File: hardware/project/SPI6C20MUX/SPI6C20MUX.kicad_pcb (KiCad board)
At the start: 4 copper layers, 160 x 100 mm, 93 parts, among them J201 5499141-4, J301 Conn_01x06, J302 Conn_02x08_Odd_Even, K201 HE3621A0510, K202 HE3621A0510, K203 HE3621A0510, K204 HE3621A0510, K205 HE3621A0510, K206 HE3621A0510, K207 HE3621A0510, K208 HE3621A0510, K209 HE3621A0510, K210 HE3621A0510, K211 HE3621A0510, K212 HE3621A0510, K213 HE3621A0510, K214 HE3621A0510, K215 HE3621A0510, K216 HE3621A0510, K217 HE3621A0510, K218 HE3621A0510, K219 HE3621A0510, K220 HE3621A0510, K221 HE3621A0510, K222 HE3621A0510, K223 HE3621A0510, K224 HE3621A0510, K225 HE3621A0510, K226 HE3621A0510, K227 HE3621A0510, K228 HE3621A0510, K229 HE3621A0510, K230 HE3621A0510, K231 HE3621A0510, K232 HE3621A0510, K233 HE3621A0510, K234 HE3621A0510, K235 HE3621A0510, K236 HE3621A0510, K237 HE3621A0510, K238 HE3621A0510, K239 HE3621A0510, K240 HE3621A0510, K241 HE3621A0510, K242 HE3621A0510, K243 HE3621A0510, K244 HE3621A0510, K245 HE3621A0510, K246 HE3621A0510, K247 HE3621A0510, K248 HE3621A0510, K249 HE3621A0510, K250 HE3621A0510, K251 HE3621A0510, K252 HE3621A0510, K253 HE3621A0510, K254 HE3621A0510, K255 HE3621A0510, K256 HE3621A0510, K257 HE3621A0510, K258 HE3621A0510, K259 HE3621A0510, K260 HE3621A0510, K261 HE3621A0510, K262 HE3621A0510, K263 HE3621A0510, K264 HE3621A0510, K265 HE3621A0510, K266 HE3621A0510, U201 MCZ33996, U202 MCZ33996, U203 MCZ33996, U204 MCZ33996, U205 MCZ33996, U401 LM1117MPX-3.3

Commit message: Software and hardware development
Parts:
- added R301: 10k, Resistor_SMD:R_0603_1608Metric_Pad1.05x0.95mm_HandSolder, B.Cu at (134.5, 135.3)
- added R302: 10k, Resistor_SMD:R_0603_1608Metric_Pad1.05x0.95mm_HandSolder, B.Cu at (139.4, 135.3)
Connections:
- J302 pad 10: (no net) -> Net-(J302-Pad10)
- U201 pad 30: (no net) -> Net-(U201-Pad30)
- U201 pad 32: (no net) -> Net-(U201-Pad32)
- U202 pad 30: (no net) -> Net-(U202-Pad30)
- U202 pad 32: (no net) -> Net-(U202-Pad32)
- U203 pad 30: (no net) -> Net-(U203-Pad30)
- U203 pad 32: (no net) -> Net-(U203-Pad32)
- U204 pad 12: (no net) -> Net-(U204-Pad12)
- U204 pad 13: (no net) -> Net-(U204-Pad13)
- U204 pad 15: (no net) -> Net-(U204-Pad15)
- U204 pad 16: (no net) -> Net-(U204-Pad16)
- U204 pad 17: (no net) -> Net-(U204-Pad17)
- U204 pad 30: (no net) -> Net-(U204-Pad30)
- U204 pad 32: (no net) -> Net-(U204-Pad32)
- U204 pad 5: (no net) -> Net-(U204-Pad5)
- U205 pad 15: (no net) -> Net-(U205-Pad15)
- U205 pad 16: (no net) -> Net-(U205-Pad16)
- U205 pad 17: (no net) -> Net-(U205-Pad17)
- U205 pad 30: (no net) -> Net-(U205-Pad30)
- U205 pad 32: (no net) -> Net-(U205-Pad32)
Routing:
- net +3V3: track 61.0 -> 68.7 mm

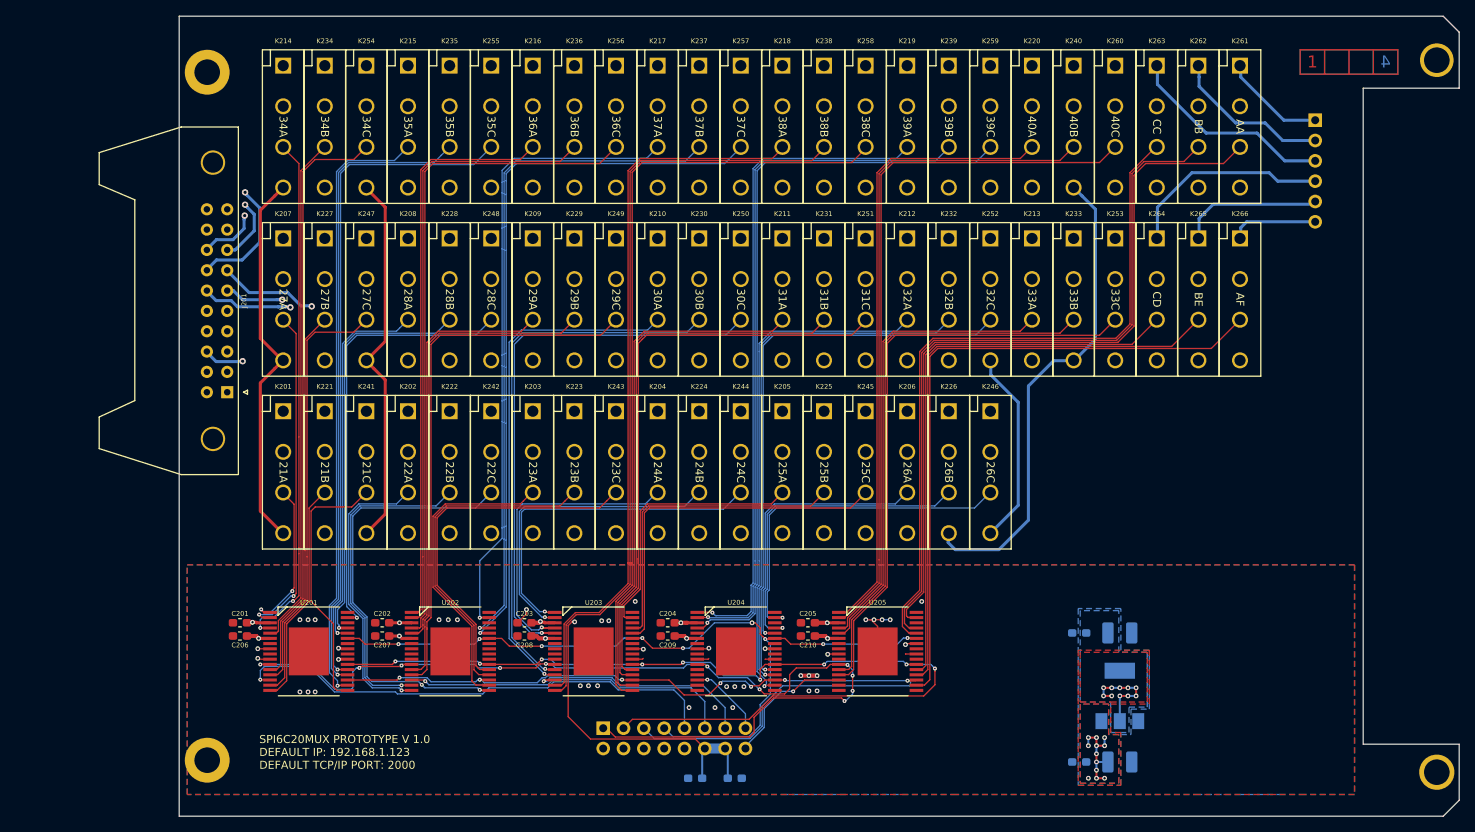
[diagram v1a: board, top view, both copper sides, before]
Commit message: PCB main and module layout.
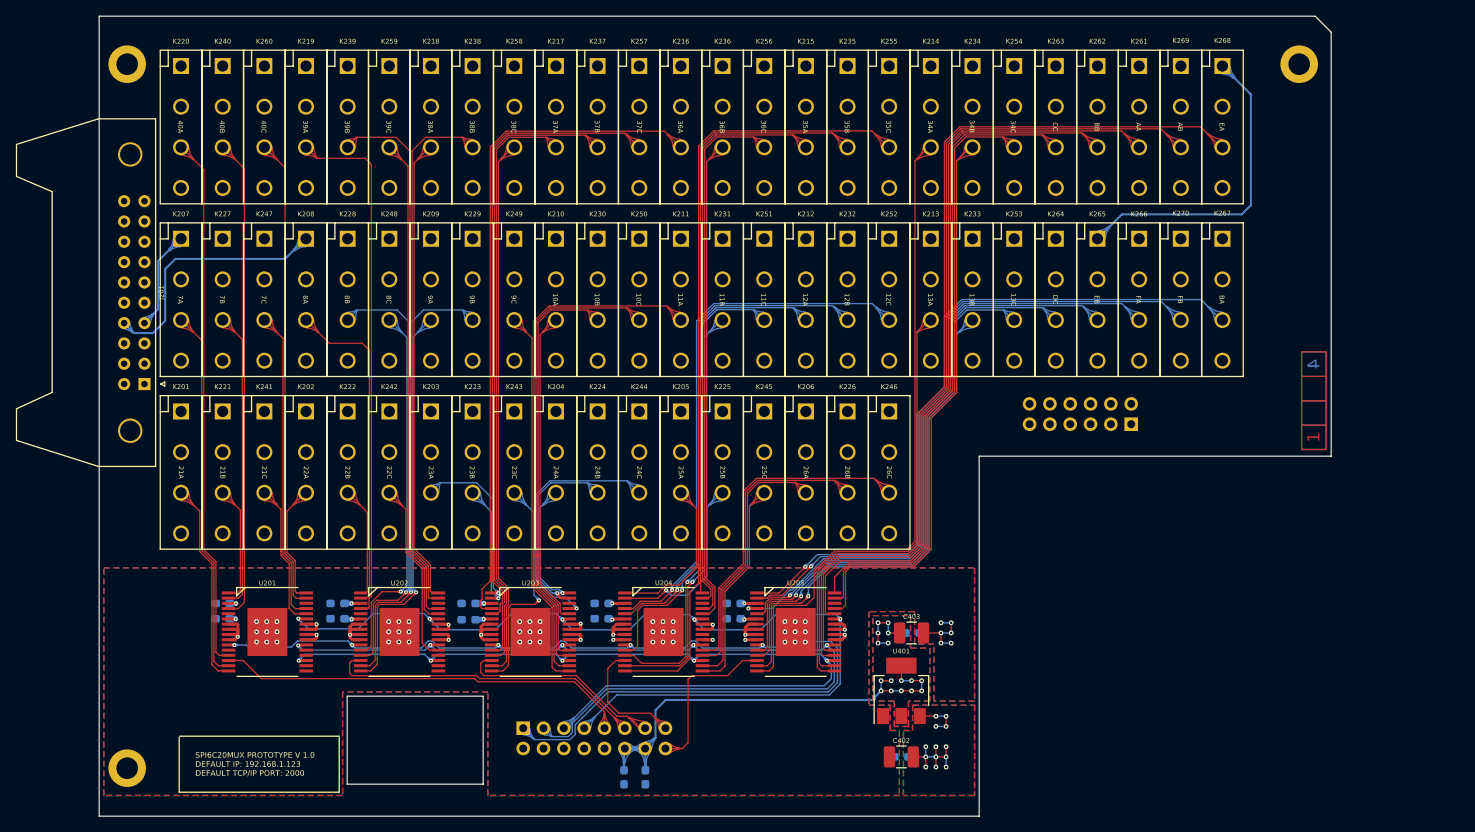
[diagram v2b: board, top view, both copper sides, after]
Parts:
- removed H104: MountingHole, MountingHole:MountingHole_3.2mm_M3_DIN965_Pad
- added K267: HE3621A0510, ETH6C20MUX:HE360_x-5331272-5, F.Cu at (200.4, 75.4)
- added K268: HE3621A0510, ETH6C20MUX:HE360_x-5331272-5, F.Cu at (200.4, 53.8)
- added K269: HE3621A0510, ETH6C20MUX:HE360_x-5331272-5, F.Cu at (195.2, 53.8)
- added K270: HE3621A0510, ETH6C20MUX:HE360_x-5331272-5, F.Cu at (195.2, 75.4)
- C201, C202, C203, C204, C205, C206, C207, C208, C209, C210: moved to B.Cu
- C402, C403, U401: moved to F.Cu
- H101, H102, H103: footprint MountingHole:MountingHole_3.2mm_M3_DIN965_Pad -> MountingHole:MountingHole_2.7mm_M2.5_DIN965_Pad
- J301: value Conn_01x06 -> Conn_02x06_Odd_Even; footprint Connector_PinHeader_2.54mm:PinHeader_1x06_P2.54mm_Vertical -> Connector_PinHeader_2.54mm:PinHeader_2x06_P2.54mm_Vertical
- moved K220 106.4 mm to (70.2, 53.8)
- moved K240 106.4 mm to (75.4, 53.8)
- moved K260 106.4 mm to (80.6, 53.8)
- moved K254 81.0 mm to (174.4, 53.8)
- moved K234 81.0 mm to (169.2, 53.8)
- moved K214 81.0 mm to (164.0, 53.8)
- moved K219 75.1 mm to (85.9, 53.8)
- moved K239 75.1 mm to (91.1, 53.8)
- moved K259 75.1 mm to (96.3, 53.8)
- moved K255 49.8 mm to (158.8, 53.8)
- moved K215 49.7 mm to (148.3, 53.8)
- moved K235 49.7 mm to (153.5, 53.8)
- moved J301 44.4 mm to (189.0, 91.0), turned to 90 degrees
- moved K218 43.9 mm to (101.5, 53.8)
- moved K238 43.9 mm to (106.7, 53.8)
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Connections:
- J301 pad 2: /Connector/B -> /Connector/A
- J301 pad 3: /Connector/C -> /Connector/B
- J301 pad 4: /Connector/D -> /Connector/B
- J301 pad 5: /Connector/E -> /Connector/C
- J301 pad 6: /Connector/F -> /Connector/C
- J302 pad 10: Net-(J302-Pad10) -> (no net)
- U201 pad 1: /Relays/RELAY21A -> /Relays/RELAY21B
- U201 pad 12: /Relays/RELAY34C -> (no net)
- U201 pad 13: /Relays/RELAY27B -> /Relays/RELAY40A
- U201 pad 15: /Relays/RELAY27C -> /Relays/RELAY27A
- U201 pad 16: /Relays/RELAY21B -> /Relays/RELAY21A
- U201 pad 17: /Relays/RELAY21C -> (no net)
- U201 pad 18: /Relays/RELAY35A -> (no net)
- U201 pad 2: /Relays/RELAY27A -> /Relays/RELAY27B
- U201 pad 20: /Relays/RELAY35B -> (no net)
- U201 pad 21: /Relays/RELAY35C -> (no net)
- U201 pad 28: /Relays/RELAY28A -> /Relays/RELAY21C
- U201 pad 29: /Relays/RELAY28B -> /Relays/RELAY27C
- U201 pad 30: Net-(U201-Pad30) -> (no net)
- U201 pad 31: /Relays/RELAY28C -> /Relays/RELAY40C
- U201 pad 32: Net-(U201-Pad32) -> /Relays/RELAY22A
- U201 pad 4: /Relays/RELAY34A -> /Relays/RELAY40B
- U201 pad 5: /Relays/RELAY34B -> (no net)
- U202 pad 1: /Relays/RELAY36A -> /Relays/RELAY22B
- U202 pad 12: /Relays/RELAY29B -> /Relays/RELAY28C
- U202 pad 13: /Relays/RELAY29C -> /Relays/RELAY28B
- U202 pad 15: /Relays/RELAY22B -> /Relays/RELAY29B
- U202 pad 16: /Relays/RELAY22A -> /Relays/RELAY29A
- U202 pad 17: /Relays/RELAY22C -> (no net)
- U202 pad 18: /Relays/RELAY23A -> (no net)
- U202 pad 2: /Relays/RELAY36B -> /Relays/RELAY28A
- U202 pad 20: /Relays/RELAY23B -> (no net)
- U202 pad 21: /Relays/RELAY23C -> /Relays/RELAY22C
- U202 pad 28: /Relays/RELAY37C -> /Relays/RELAY39C
- U202 pad 29: /Relays/RELAY37B -> /Relays/RELAY39B
- U202 pad 30: Net-(U202-Pad30) -> (no net)
- U202 pad 31: /Relays/RELAY37A -> /Relays/RELAY38B
- U202 pad 32: Net-(U202-Pad32) -> /Relays/RELAY38A
- U202 pad 4: /Relays/RELAY36C -> /Relays/RELAY39A
- U202 pad 5: /Relays/RELAY29A -> (no net)
- U203 pad 1: /Relays/RELAY24C -> /Relays/RELAY23A
- U203 pad 12: /Relays/RELAY30B -> /Relays/RELAY37B
- U203 pad 13: /Relays/RELAY30A -> /Relays/RELAY37A
- U203 pad 15: /Relays/RELAY38A -> /Relays/RELAY38C
- U203 pad 16: /Relays/RELAY38B -> /Relays/RELAY23C
- U203 pad 17: /Relays/RELAY38C -> /Relays/RELAY29C
- U203 pad 2: /Relays/RELAY24B -> /Relays/RELAY23B
- U203 pad 20: /Relays/RELAY31B -> /Relays/RELAY30C
- U203 pad 21: /Relays/RELAY31C -> /Relays/RELAY30B
- U203 pad 28: /Relays/RELAY25C -> /Relays/RELAY30A
- U203 pad 29: /Relays/RELAY25B -> /Relays/RELAY24C
- U203 pad 30: Net-(U203-Pad30) -> (no net)
- U203 pad 31: /Relays/RELAY25A -> /Relays/RELAY24B
- U203 pad 32: Net-(U203-Pad32) -> /Relays/RELAY24A
- U203 pad 4: /Relays/RELAY24A -> /Relays/RELAY36A
- U203 pad 5: /Relays/RELAY30C -> /Relays/RELAY37C
- U204 pad 1: /Relays/RELAY39A -> /Relays/RELAY25A
- U204 pad 12: Net-(U204-Pad12) -> /Relays/RELAY32A
- U204 pad 13: Net-(U204-Pad13) -> /Relays/RELAY31C
- U204 pad 15: Net-(U204-Pad15) -> /Relays/RELAY31B
- U204 pad 16: Net-(U204-Pad16) -> /Relays/RELAY35C
- U204 pad 17: Net-(U204-Pad17) -> /Relays/RELAY25C
- U204 pad 18: /Relays/RELAY32A -> /Relays/RELAY26A
- U204 pad 2: /Relays/RELAY39B -> /Relays/RELAY25B
- U204 pad 20: /Relays/RELAY32B -> /Relays/RELAY26B
- U204 pad 21: /Relays/RELAY32C -> /Relays/RELAY26C
- U204 pad 28: /Relays/RELAY26A -> /Relays/RELAY36B
- U204 pad 29: /Relays/RELAY26B -> /Relays/RELAY36C
- U204 pad 30: Net-(U204-Pad30) -> (no net)
- U204 pad 31: /Relays/RELAY26C -> /Relays/RELAY35A
- U204 pad 32: Net-(U204-Pad32) -> /Relays/RELAY35B
- U204 pad 4: /Relays/RELAY39C -> /Relays/RELAY32C
- U204 pad 5: Net-(U204-Pad5) -> /Relays/RELAY32B
- U205 pad 1: /Relays/RELAY40A -> /Relays/RELAYBA
- U205 pad 12: /Relays/RELAY33B -> /Relays/RELAYD
- U205 pad 15: Net-(U205-Pad15) -> /Relays/RELAY33B
- U205 pad 16: Net-(U205-Pad16) -> /Relays/RELAY34A
- U205 pad 17: Net-(U205-Pad17) -> /Relays/RELAY33A
- U205 pad 18: /Relays/RELAYF -> /Relays/RELAYEA
- U205 pad 2: /Relays/RELAY40B -> /Relays/RELAYFA
- U205 pad 20: /Relays/RELAYE -> /Relays/RELAYAB
- U205 pad 21: /Relays/RELAYD -> /Relays/RELAYA
- U205 pad 28: /Relays/RELAYC -> /Relays/RELAYB
- U205 pad 29: /Relays/RELAYB -> /Relays/RELAY34B
- U205 pad 30: Net-(U205-Pad30) -> (no net)
- U205 pad 31: /Relays/RELAYA -> /Relays/RELAY34C
- U205 pad 32: Net-(U205-Pad32) -> /Relays/RELAYC
- U205 pad 4: /Relays/RELAY40C -> /Relays/RELAYF
- U205 pad 5: /Relays/RELAY33A -> /Relays/RELAYE
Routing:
- net /Relays/RELAYEA: track 0.00 -> 115.0 mm
- net /Relays/RELAYAB: track 0.00 -> 107.8 mm
- net /Relays/PIN40: track 131.5 -> 31.4 mm
- net /Relays/RELAYBA: track 0.00 -> 89.1 mm, vias 0 -> 1
- net /Relays/PIN34: track 44.5 -> 131.7 mm, vias 1 -> 0
- net /Relays/RELAYFA: track 0.00 -> 84.0 mm, vias 0 -> 1
- net /Relays/PIN21C: track 450.2 -> 369.8 mm
- net /Connector/C: track 25.9 -> 99.6 mm
- net /Relays/PIN39: track 113.7 -> 43.7 mm
- net GND: track 31.0 -> 98.1 mm, vias 41 -> 68
- net /Connector/A: track 12.8 -> 71.3 mm
- net /Relays/PIN35: track 53.8 -> 109.7 mm, vias 1 -> 0
- net /Connector/E: track 17.8 -> 66.8 mm
- net /Connector/B: track 19.8 -> 66.1 mm
- net /Relays/PIN38: track 101.5 -> 64.0 mm
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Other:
- board size 160 x 100 mm -> 154 x 100 mm
- board text added: "10A"
- board text added: "10B"
- board text added: "10C"
- board text added: "11A"
- board text added: "11B"
- board text added: "11C"
- board text added: "12A"
- board text added: "12B"
- board text added: "12C"
- board text added: "13A"
- board text added: "13B"
- board text added: "13C"
- board text added: "14A"
- board text added: "14B"
- board text added: "14C"
- board text added: "15A"
- board text added: "15B"
- board text added: "15C"
- board text added: "16A"
- board text added: "16B"
- board text added: "16C"
- board text added: "17A"
- board text added: "17B"
- board text added: "17C"
- board text added: "18A"
- board text added: "18B"
- board text added: "18C"
- board text added: "19A"
- board text added: "19B"
- board text added: "19C"
- board text added: "1A"
- board text added: "1B"
- board text added: "1C"
- board text added: "20A"
- board text added: "20B"
- board text added: "20C"
- board text added: "2A"
- board text added: "2B"
- board text added: "2C"
- board text added: "3A"
- board text added: "3B"
- board text added: "3C"
- board text added: "4A"
- board text added: "4B"
- board text added: "4C"
- board text added: "5A"
- board text added: "5B"
- board text added: "5C"
- board text added: "6A"
- board text added: "6B"
- board text added: "6C"
- board text added: "7A"
- board text added: "7B"
- board text added: "7C"
- board text added: "8A"
- board text added: "8B"
- board text added: "8C"
- board text added: "9A"
- board text added: "9B"
- board text added: "9C"
- board text added: "AB"
- board text added: "BA"
- board text added: "DC"
- board text added: "EA"
- board text added: "EB"
- board text added: "FA"
- board text added: "FB"
- board text removed: "27A"
- board text removed: "27B"
- board text removed: "27C"
- board text removed: "28A"
- board text removed: "28B"
- board text removed: "28C"
- board text removed: "29A"
- board text removed: "29B"
- board text removed: "29C"
- board text removed: "30A"
- board text removed: "30B"
- board text removed: "30C"
- board text removed: "31A"
- board text removed: "31B"
- board text removed: "31C"
- board text removed: "32A"
- board text removed: "32B"
- board text removed: "32C"
- board text removed: "33A"
- board text removed: "33B"
- board text removed: "33C"
- board text removed: "AF"
- board text removed: "BE"
- board text removed: "CD"

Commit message: PCB layouts done.
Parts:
- moved C401 20.1 mm to (171.2, 115.7), turned to 270 degrees
- moved C402 20.1 mm to (171.2, 115.7), turned to 270 degrees
- moved U401 8.41 mm to (164.1, 116.8), turned to 180 degrees
- moved C404 5.28 mm to (156.5, 118.0), turned to 270 degrees
- moved C403 5.16 mm to (156.5, 118.0), turned to 270 degrees
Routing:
- net (no net): track 0.00 -> 85.9 mm
- net GND: track 98.1 -> 93.6 mm, vias 68 -> 65
- net +5V: track 28.0 -> 23.4 mm, vias 18 -> 15
- net /Connector/RELAY2_~RST: track 121.1 -> 120.2 mm
- net +3V3: track 74.6 -> 73.8 mm, vias 21 -> 15
- net /Connector/RELAY2_~CS4: track 20.6 -> 20.0 mm
- net /Relays/RELAYC: track 80.5 -> 81.0 mm
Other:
- outline, holes or cut-outs redrawn
- board text added: "27A"
- board text added: "27B"
- board text added: "27C"
- board text added: "28A"
- board text added: "28B"
- board text added: "28C"
- board text added: "29A"
- board text added: "29B"
- board text added: "29C"
- board text added: "30A"
- board text added: "30B"
- board text added: "30C"
- board text added: "31A"
- board text added: "31B"
- board text added: "31C"
- board text added: "32A"
- board text added: "32B"
- board text added: "32C"
- board text added: "33A"
- board text added: "33B"
- board text added: "33C"
- board text removed: "10A"
- board text removed: "10B"
- board text removed: "10C"
- board text removed: "11A"
- board text removed: "11B"
- board text removed: "11C"
- board text removed: "12A"
- board text removed: "12B"
- board text removed: "12C"
- board text removed: "13A"
- board text removed: "13B"
- board text removed: "13C"
- board text removed: "14A"
- board text removed: "14B"
- board text removed: "14C"
- board text removed: "15A"
- board text removed: "15B"
- board text removed: "15C"
- board text removed: "16A"
- board text removed: "16B"
- board text removed: "16C"
- board text removed: "17A"
- board text removed: "17B"
- board text removed: "17C"
- board text removed: "18A"
- board text removed: "18B"
- board text removed: "18C"
- board text removed: "19A"
- board text removed: "19B"
- board text removed: "19C"
- board text removed: "1A"
- board text removed: "1B"
- board text removed: "1C"
- board text removed: "20A"
- board text removed: "20B"
- board text removed: "20C"
- board text removed: "2A"
- board text removed: "2B"
- board text removed: "2C"
- board text removed: "3A"
- board text removed: "3B"
- board text removed: "3C"
- board text removed: "4A"
- board text removed: "4B"
- board text removed: "4C"
- board text removed: "5A"
- board text removed: "5B"
- board text removed: "5C"
- board text removed: "6A"
- board text removed: "6B"
- board text removed: "6C"
- board text removed: "7A"
- board text removed: "7B"
- board text removed: "7C"
- board text removed: "8A"
- board text removed: "8B"
- board text removed: "8C"
- board text removed: "9A"
- board text removed: "9B"
- board text removed: "9C"

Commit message: PCB modifications.
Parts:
- moved C403 2.30 mm to (156.2, 115.7)
- moved C404 2.30 mm to (156.2, 115.7)
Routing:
- net +3V3: track 73.8 -> 75.7 mm
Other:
- outline, holes or cut-outs redrawn
